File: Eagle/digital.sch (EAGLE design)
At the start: 44 parts, among them J1 USB-B

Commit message: Added indicator LEDs
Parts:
- added LED2, LED3: (no value), led:LED3MM
- added R16, R17: 200k, resistor:R-US_0204/2V
- JP1: device jumper:JP1Q -> jumper:JP2E
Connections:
- new net N$41: LED2.A, R16.1
- new net N$42: LED3.A, R17.1
- new net N$43: J1.VBUS, R17.2
- new net N$45: C3.1, C4.1, C5.1, JP1.2, U$1.VDD$1, U$1.VDD$2
- net +5V/2: now also JP1.3, R16.2; no longer C3.1, C4.1, C5.1, JP1.2, U$1.VDD$1, U$1.VDD$2
- net DGND: now also LED2.C, LED3.C
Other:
- moved on the sheet: C4, C5
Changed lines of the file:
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@@
 <part name="SUPPLY3" library="supply2" deviceset="+5V/2" device=""/>
 <part name="SUPPLY20" library="supply2" deviceset="+5V/2" device=""/>
-<part name="SUPPLY7" library="supply2" deviceset="+5V/2" device=""/>
-<part name="SUPPLY9" library="supply2" deviceset="+5V/2" device=""/>
-<part name="SUPPLY4" library="supply2" deviceset="+5V/2" device=""/>
 <part name="X1" library="con-subd" deviceset="M25?S" device="H"/>
-<part name="JP1" library="jumper" deviceset="JP1Q" device=""/>
 <part name="SUPPLY11" library="supply2" deviceset="+5V/2" device=""/>
 <part name="SUPPLY12" library="supply2" deviceset="GND" device=""/>
@@
 <part name="SUPPLY56" library="supply2" deviceset="DGND" device=""/>
 <part name="SUPPLY57" library="supply2" deviceset="DGND" device=""/>
+<part name="R16" library="resistor" deviceset="R-US_" device="0204/2V" value="200k"/>
+<part name="LED2" library="led" deviceset="LED" device="3MM"/>
+<part name="R17" library="resistor" deviceset="R-US_" device="0204/2V" value="200k"/>
+<part name="LED3" library="led" deviceset="LED" device="3MM"/>
+<part name="SUPPLY58" library="supply2" deviceset="DGND" device=""/>
+<part name="JP1" library="jumper" deviceset="JP2E" device=""/>
 </parts>
 <sheets>
@@
 <instance part="J1" gate="G$1" x="71.12" y="0"/>
 <instance part="C3" gate="G$1" x="45.72" y="111.76"/>
-<instance part="C4" gate="G$1" x="15.24" y="129.54"/>
-<instance part="C5" gate="G$1" x="27.94" y="132.08"/>
+<instance part="C4" gate="G$1" x="-7.62" y="88.9"/>
+<instance part="C5" gate="G$1" x="5.08" y="88.9"/>
 <instance part="SUPPLY13" gate="GND" x="147.32" y="-96.52"/>
 <instance part="CN1" gate="G$1" x="355.6" y="-17.78" rot="MR0"/>
@@
 <instance part="SUPPLY17" gate="G$1" x="35.56" y="-15.24"/>
 <instance part="SUPPLY1" gate="G$1" x="-2.54" y="35.56"/>
-<instance part="SUPPLY5" gate="G$1" x="0" y="91.44"/>
+<instance part="SUPPLY5" gate="G$1" x="-20.32" y="91.44"/>
 <instance part="SUPPLY6" gate="G$1" x="68.58" y="-5.08"/>
-<instance part="SUPPLY8" gate="G$1" x="15.24" y="121.92"/>
-<instance part="SUPPLY10" gate="G$1" x="27.94" y="124.46"/>
+<instance part="SUPPLY8" gate="G$1" x="-7.62" y="78.74"/>
+<instance part="SUPPLY10" gate="G$1" x="5.08" y="78.74"/>
 <instance part="SUPPLY18" gate="G$1" x="325.12" y="-30.48"/>
 <instance part="C12" gate="G$1" x="254" y="-17.78"/>
@@
 <instance part="SUPPLY19" gate="+5V" x="218.44" y="-5.08"/>
 <instance part="SUPPLY3" gate="G$1" x="304.8" y="-5.08"/>
-<instance part="SUPPLY20" gate="G$1" x="35.56" y="111.76"/>
-<instance part="SUPPLY7" gate="G$1" x="15.24" y="134.62"/>
-<instance part="SUPPLY9" gate="G$1" x="27.94" y="137.16"/>
-<instance part="SUPPLY4" gate="G$1" x="-2.54" y="124.46"/>
+<instance part="SUPPLY20" gate="G$1" x="40.64" y="116.84" rot="R270"/>
 <instance part="X1" gate="-1" x="149.86" y="-78.74"/>
 <instance part="X1" gate="-4" x="149.86" y="-81.28"/>
@@
 <instance part="X1" gate="-25" x="-60.96" y="12.7" rot="R180"/>
 <instance part="X1" gate="-17" x="215.9" y="-7.62" rot="R180"/>
-<instance part="JP1" gate="A" x="-2.54" y="114.3"/>
 <instance part="SUPPLY11" gate="G$1" x="106.68" y="124.46"/>
 <instance part="SUPPLY12" gate="GND" x="124.46" y="114.3"/>
@@
 <instance part="SUPPLY56" gate="G$1" x="96.52" y="-2.54"/>
 <instance part="SUPPLY57" gate="G$1" x="96.52" y="-17.78"/>
+<instance part="R16" gate="G$1" x="347.98" y="-12.7" rot="R90"/>
+<instance part="LED2" gate="G$1" x="347.98" y="-20.32"/>
+<instance part="R17" gate="G$1" x="63.5" y="-2.54" rot="R90"/>
+<instance part="LED3" gate="G$1" x="63.5" y="-10.16"/>
+<instance part="SUPPLY58" gate="G$1" x="63.5" y="-17.78"/>
+<instance part="JP1" gate="1" x="35.56" y="119.38"/>
 </instances>
 <busses>
@@
 <segment>
 <pinref part="U$2" gate="G$1" pin="GND"/>
-<wire x1="-33.02" y1="93.98" x2="0" y2="93.98" width="0.1524" layer="91"/>
+<wire x1="-33.02" y1="93.98" x2="-20.32" y2="93.98" width="0.1524" layer="91"/>
 <pinref part="SUPPLY5" gate="G$1" pin="DGND"/>
 </segment>
@@
 <pinref part="C4" gate="G$1" pin="2"/>
 <pinref part="SUPPLY8" gate="G$1" pin="DGND"/>
+<wire x1="-7.62" y1="81.28" x2="-7.62" y2="83.82" width="0.1524" layer="91"/>
 </segment>
 <segment>
 <pinref part="C5" gate="G$1" pin="2"/>
 <pinref part="SUPPLY10" gate="G$1" pin="DGND"/>
+<wire x1="5.08" y1="81.28" x2="5.08" y2="83.82" width="0.1524" layer="91"/>
 </segment>
 <segment>
 <pinref part="CN1" gate="G$1" pin="GND"/>
 <wire x1="353.06" y1="-20.32" x2="353.06" y2="-27.94" width="0.1524" layer="91"/>
-<wire x1="353.06" y1="-27.94" x2="337.82" y2="-27.94" width="0.1524" layer="91"/>
+<wire x1="353.06" y1="-27.94" x2="347.98" y2="-27.94" width="0.1524" layer="91"/>
 <pinref part="D1" gate="G$1" pin="A"/>
+<wire x1="347.98" y1="-27.94" x2="337.82" y2="-27.94" width="0.1524" layer="91"/>
 <wire x1="337.82" y1="-27.94" x2="325.12" y2="-27.94" width="0.1524" layer="91"/>
 <wire x1="337.82" y1="-20.32" x2="337.82" y2="-27.94" width="0.1524" layer="91"/>
@@
 <junction x="312.42" y="-27.94"/>
 <pinref part="SUPPLY18" gate="G$1" pin="DGND"/>
+<pinref part="LED2" gate="G$1" pin="C"/>
+<wire x1="347.98" y1="-25.4" x2="347.98" y2="-27.94" width="0.1524" layer="91"/>
+<junction x="347.98" y="-27.94"/>
 </segment>
 <segment>
@@
 <pinref part="OK7" gate="B" pin="C"/>
 <pinref part="SUPPLY57" gate="G$1" pin="DGND"/>
+</segment>
+<segment>
+<pinref part="LED3" gate="G$1" pin="C"/>
+<pinref part="SUPPLY58" gate="G$1" pin="DGND"/>
 </segment>
 </net>
@@
 <pinref part="CN1" gate="G$1" pin="PWR"/>
 <wire x1="353.06" y1="-15.24" x2="353.06" y2="-7.62" width="0.1524" layer="91"/>
-<wire x1="353.06" y1="-7.62" x2="337.82" y2="-7.62" width="0.1524" layer="91"/>
+<wire x1="353.06" y1="-7.62" x2="347.98" y2="-7.62" width="0.1524" layer="91"/>
 <pinref part="D1" gate="G$1" pin="C"/>
+<wire x1="347.98" y1="-7.62" x2="337.82" y2="-7.62" width="0.1524" layer="91"/>
 <wire x1="337.82" y1="-7.62" x2="325.12" y2="-7.62" width="0.1524" layer="91"/>
 <wire x1="337.82" y1="-15.24" x2="337.82" y2="-7.62" width="0.1524" layer="91"/>
@@
 <pinref part="SUPPLY3" gate="G$1" pin="+5V/2"/>
 <junction x="304.8" y="-7.62"/>
-</segment>
-<segment>
-<pinref part="U$1" gate="G$1" pin="VDD$1"/>
-<wire x1="35.56" y1="109.22" x2="35.56" y2="106.68" width="0.1524" layer="91"/>
-<pinref part="U$1" gate="G$1" pin="VDD$2"/>
-<wire x1="35.56" y1="106.68" x2="38.1" y2="106.68" width="0.1524" layer="91"/>
-<junction x="35.56" y="106.68"/>
-<wire x1="38.1" y1="106.68" x2="40.64" y2="106.68" width="0.1524" layer="91"/>
-<wire x1="40.64" y1="106.68" x2="40.64" y2="114.3" width="0.1524" layer="91"/>
-<junction x="38.1" y="106.68"/>
-<pinref part="C3" gate="G$1" pin="1"/>
-<wire x1="40.64" y1="114.3" x2="45.72" y2="114.3" width="0.1524" layer="91"/>
-<pinref part="SUPPLY20" gate="G$1" pin="+5V/2"/>
-</segment>
-<segment>
-<pinref part="C4" gate="G$1" pin="1"/>
-<pinref part="SUPPLY7" gate="G$1" pin="+5V/2"/>
-</segment>
-<segment>
-<pinref part="C5" gate="G$1" pin="1"/>
-<pinref part="SUPPLY9" gate="G$1" pin="+5V/2"/>
-</segment>
-<segment>
-<pinref part="JP1" gate="A" pin="2"/>
-<pinref part="SUPPLY4" gate="G$1" pin="+5V/2"/>
+<pinref part="R16" gate="G$1" pin="2"/>
+<junction x="347.98" y="-7.62"/>
 </segment>
 <segment>
@@
 <pinref part="SUPPLY47" gate="G$1" pin="+5V/2"/>
 </segment>
+<segment>
+<pinref part="SUPPLY20" gate="G$1" pin="+5V/2"/>
+<pinref part="JP1" gate="1" pin="3"/>
+</segment>
 </net>
 <net name="N$10" class="0">
 <segment>
 <pinref part="U$2" gate="G$1" pin="VCC"/>
-<pinref part="JP1" gate="A" pin="1"/>
 <wire x1="-33.02" y1="96.52" x2="-2.54" y2="96.52" width="0.1524" layer="91"/>
-<wire x1="-2.54" y1="96.52" x2="-2.54" y2="106.68" width="0.1524" layer="91"/>
+<wire x1="-2.54" y1="96.52" x2="-2.54" y2="109.22" width="0.1524" layer="91"/>
+<wire x1="33.02" y1="116.84" x2="33.02" y2="109.22" width="0.1524" layer="91"/>
+<wire x1="33.02" y1="109.22" x2="-2.54" y2="109.22" width="0.1524" layer="91"/>
+<pinref part="JP1" gate="1" pin="1"/>
 </segment>
 </net>
@@
 </segment>
 </net>
+<net name="N$41" class="0">
+<segment>
+<pinref part="R16" gate="G$1" pin="1"/>
+<pinref part="LED2" gate="G$1" pin="A"/>
+</segment>
+</net>
+<net name="N$42" class="0">
+<segment>
+<pinref part="R17" gate="G$1" pin="1"/>
+<pinref part="LED3" gate="G$1" pin="A"/>
+</segment>
+</net>
+<net name="N$43" class="0">
+<segment>
+<pinref part="J1" gate="G$1" pin="VBUS"/>
+<pinref part="R17" gate="G$1" pin="2"/>
+<wire x1="68.58" y1="2.54" x2="63.5" y2="2.54" width="0.1524" layer="91"/>
+</segment>
+</net>
+<net name="N$45" class="0">
+<segment>
+<pinref part="C4" gate="G$1" pin="1"/>
+<pinref part="C5" gate="G$1" pin="1"/>
+<wire x1="-7.62" y1="91.44" x2="2.54" y2="91.44" width="0.1524" layer="91"/>
+<wire x1="2.54" y1="91.44" x2="5.08" y2="91.44" width="0.1524" layer="91"/>
+<wire x1="2.54" y1="91.44" x2="2.54" y2="106.68" width="0.1524" layer="91"/>
+<junction x="2.54" y="91.44"/>
+<pinref part="U$1" gate="G$1" pin="VDD$1"/>
+<pinref part="U$1" gate="G$1" pin="VDD$2"/>
+<wire x1="35.56" y1="106.68" x2="38.1" y2="106.68" width="0.1524" layer="91"/>
+<wire x1="38.1" y1="106.68" x2="40.64" y2="106.68" width="0.1524" layer="91"/>
+<wire x1="40.64" y1="106.68" x2="40.64" y2="114.3" width="0.1524" layer="91"/>
+<junction x="38.1" y="106.68"/>
+<pinref part="C3" gate="G$1" pin="1"/>
+<wire x1="40.64" y1="114.3" x2="45.72" y2="114.3" width="0.1524" layer="91"/>
+<pinref part="JP1" gate="1" pin="2"/>
+<wire x1="35.56" y1="116.84" x2="35.56" y2="106.68" width="0.1524" layer="91"/>
+<junction x="35.56" y="106.68"/>
+<wire x1="2.54" y1="106.68" x2="35.56" y2="106.68" width="0.1524" layer="91"/>
+</segment>
+</net>

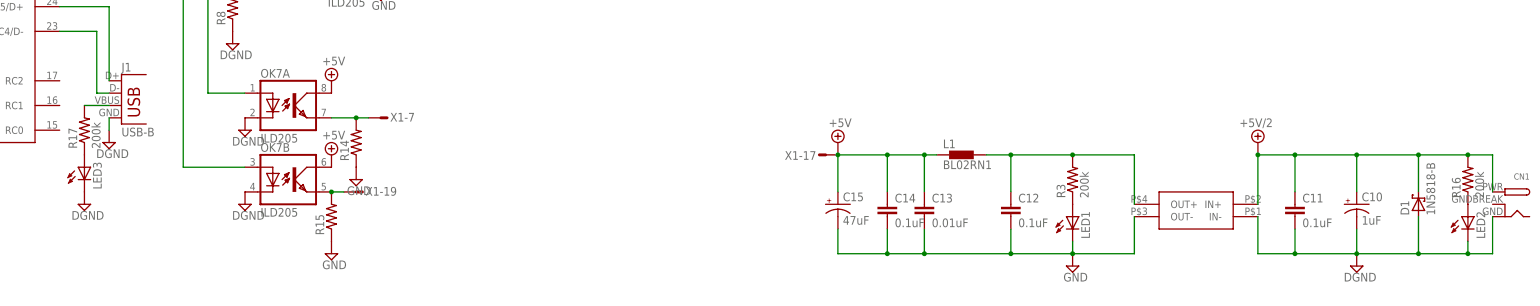
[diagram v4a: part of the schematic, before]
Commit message: Updated resistor values
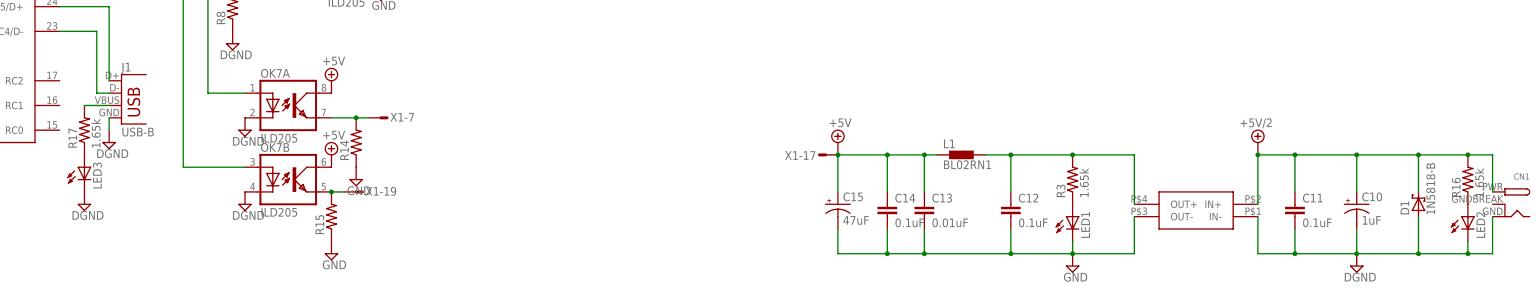
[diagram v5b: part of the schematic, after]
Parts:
- R16, R17, R3: value 200k -> 1.65k
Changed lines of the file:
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@@
 <part name="C11" library="resistor" deviceset="C-EU" device="050-025X075" value="0.1uF"/>
 <part name="U$3" library="modEEG" deviceset="ROL-0505S" device=""/>
-<part name="R3" library="resistor" deviceset="R-US_" device="0204/2V" value="200k"/>
+<part name="R3" library="resistor" deviceset="R-US_" device="0204/2V" value="1.65k"/>
 <part name="LED1" library="led" deviceset="LED" device="3MM"/>
 <part name="SUPPLY2" library="supply2" deviceset="GND" device=""/>
@@
 <part name="SUPPLY56" library="supply2" deviceset="DGND" device=""/>
 <part name="SUPPLY57" library="supply2" deviceset="DGND" device=""/>
-<part name="R16" library="resistor" deviceset="R-US_" device="0204/2V" value="200k"/>
+<part name="R16" library="resistor" deviceset="R-US_" device="0204/2V" value="1.65k"/>
 <part name="LED2" library="led" deviceset="LED" device="3MM"/>
-<part name="R17" library="resistor" deviceset="R-US_" device="0204/2V" value="200k"/>
+<part name="R17" library="resistor" deviceset="R-US_" device="0204/2V" value="1.65k"/>
 <part name="LED3" library="led" deviceset="LED" device="3MM"/>
 <part name="SUPPLY58" library="supply2" deviceset="DGND" device=""/>

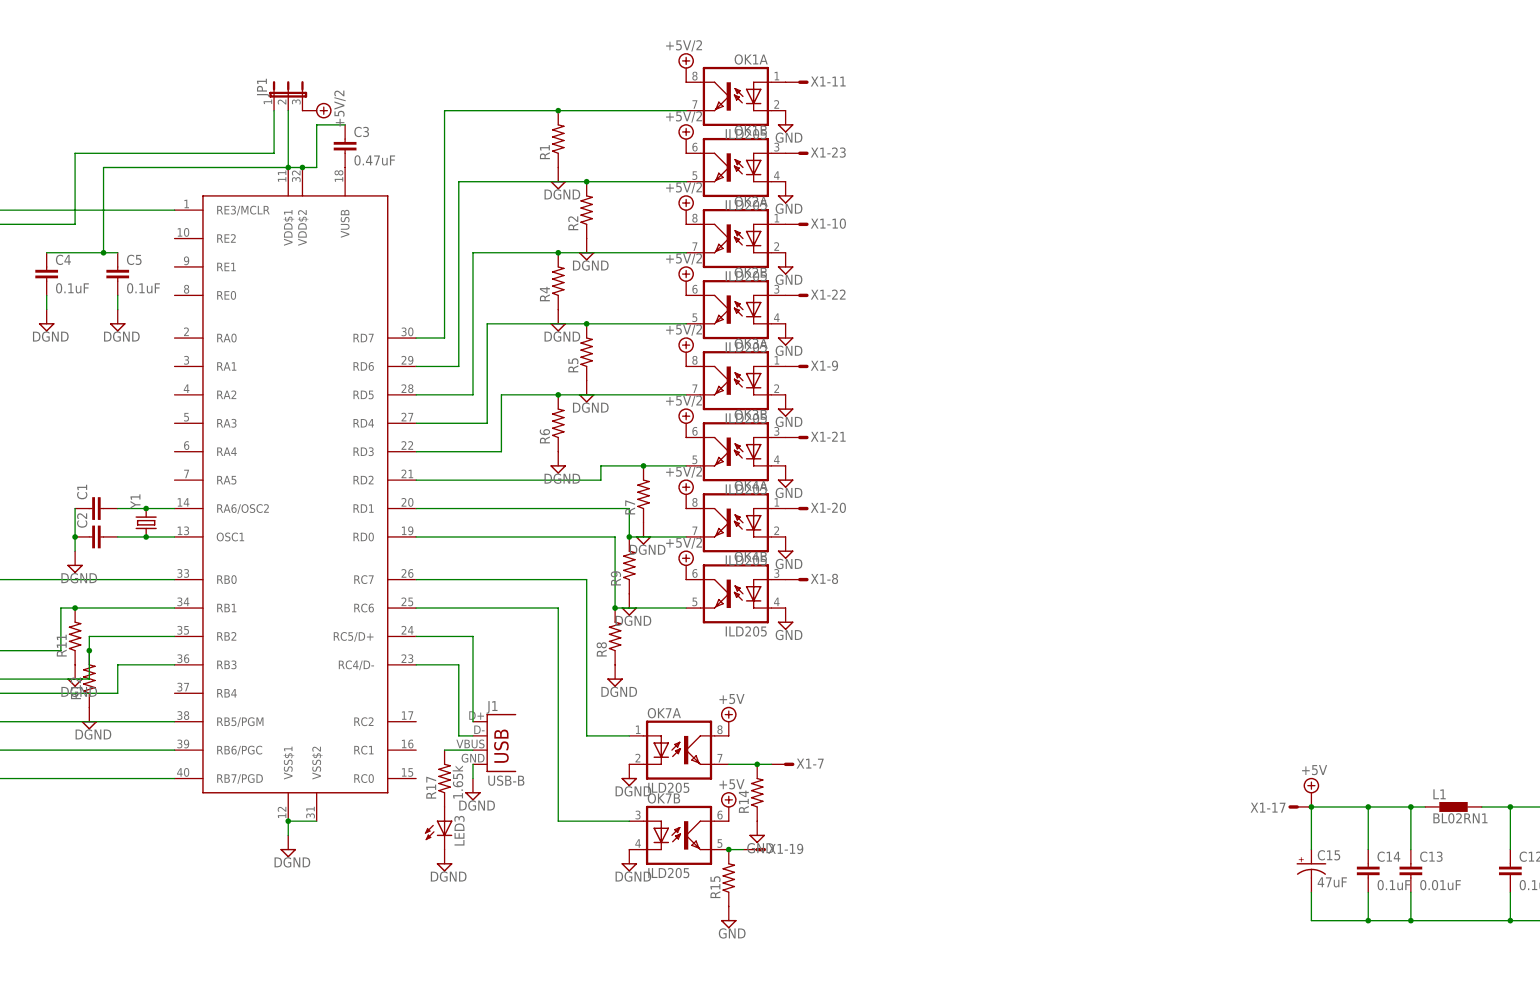
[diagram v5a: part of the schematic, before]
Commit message: Added 232 interface
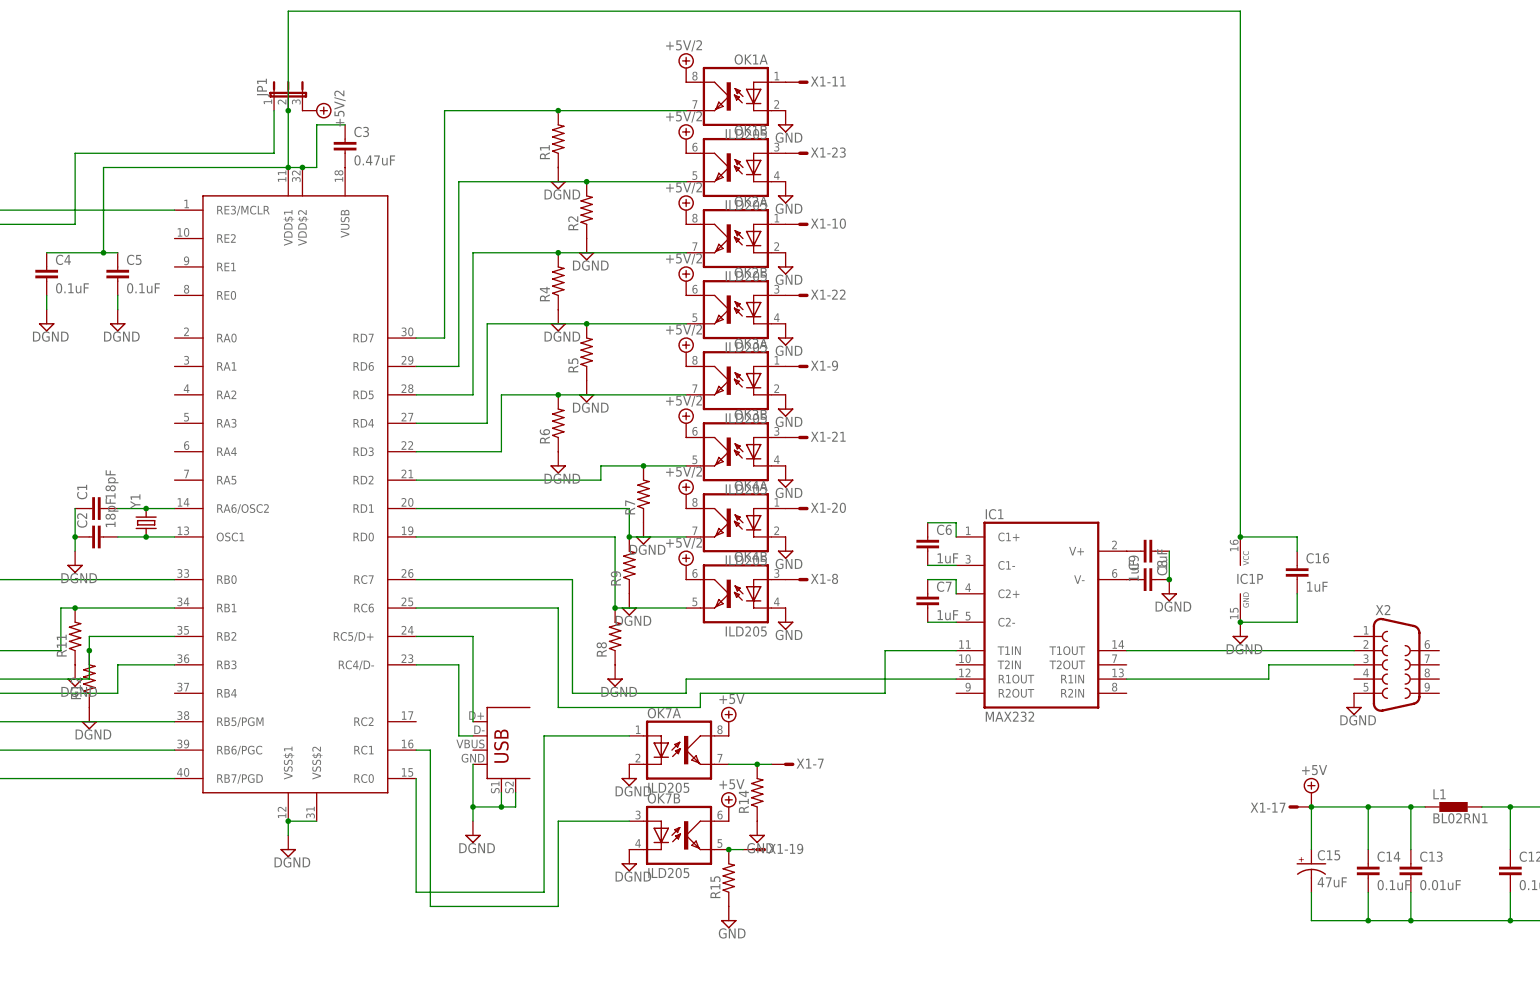
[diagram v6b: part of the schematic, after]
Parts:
- removed LED3: (no value), led:LED3MM
- removed R17: 1.65k, resistor:R-US_0204/2V
- added C16, C6, C7, C8, C9: 1uF, resistor:C-EU050-025X075
- added IC1: MAX232, maxim:MAX232
- added X2: (no value), con-subd:F09HP
- C1, C2: value (none) -> 18pF
- J1: value USB-B -> USB+SHIELD; device SparkFun-Connectors:USBPTH -> SparkFun-Connectors:USB+SHIELD
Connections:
- removed net N$42: LED3.A, R17.1
- removed net N$43: J1.VBUS, R17.2
- new net N$44: IC1G$1.T1IN, U$1.RC6
- new net N$46: IC1G$1.R1OUT, U$1.RC7
- new net N$47: C8.2, IC1G$1.V+
- new net N$48: C9.1, IC1G$1.V-
- new net N$49: C6.2, IC1G$1.C1-
- new net N$50: C6.1, IC1G$1.C1+
- new net N$51: C7.1, IC1G$1.C2+
- new net N$52: C7.2, IC1G$1.C2-
- new net N$53: IC1G$1.R1IN, X2.3
- new net N$54: IC1G$1.T1OUT, X2.2
- net DGND: now also C16.2, C8.1, C9.2, IC1P.GND, J1.S1, J1.S2, X2.5; no longer LED3.C
- net N$39: now also U$1.RC0; no longer U$1.RC7
- net N$40: now also U$1.RC1; no longer U$1.RC6
- net N$45: now also C16.1, IC1P.VCC

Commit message: Changed USB to differential pair
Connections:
- net N$3 renamed USB_P
- net N$4 renamed USB_N
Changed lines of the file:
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@@
 <class number="0" name="default" width="0" drill="0">
+</class>
+<class number="1" name="USB" width="0.3048" drill="0">
+<clearance class="1" value="2.54"/>
 </class>
 </classes>
@@
 </segment>
 </net>
-<net name="N$3" class="0">
+<net name="USB_P" class="1">
 <segment>
 <pinref part="J1" gate="G$1" pin="D+"/>
@@
 </segment>
 </net>
-<net name="N$4" class="0">
+<net name="USB_N" class="1">
 <segment>
 <pinref part="U$1" gate="G$1" pin="RC4/D-"/>

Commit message: Added ethernet module
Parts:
- removed C16, C6, C7, C8, C9: 1uF, resistor:C-EU050-025X075
- removed J1: USB+SHIELD, SparkFun-Connectors:USB+SHIELD
- removed X2: (no value), con-subd:F09HP
- added S1: (no value), switch:9070-1W
- added U$4: ENC28J60-H, modEEG:ENC28J60-H
- added U$5: USBSMD, SparkFun-Connectors:USBSMD
- IC1: value MAX232 -> L4931CZ33-AP; device maxim:MAX232 -> v-reg:LP2950ACZ-3.0
- U$2: value PIC-ICSPPOLAR_LOCK -> PIC-ICSPPTH; device SparkFun-Connectors:PIC-ICSPPOLAR_LOCK -> SparkFun-Connectors:PIC-ICSPPTH
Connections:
- removed net N$46: IC1G$1.R1OUT, U$1.RC7
- removed net N$47: C8.2, IC1G$1.V+
- removed net N$48: C9.1, IC1G$1.V-
- removed net N$49: C6.2, IC1G$1.C1-
- removed net N$50: C6.1, IC1G$1.C1+
- removed net N$51: C7.1, IC1G$1.C2+
- removed net N$52: C7.2, IC1G$1.C2-
- removed net N$53: IC1G$1.R1IN, X2.3
- removed net N$54: IC1G$1.T1OUT, X2.2
- new net N$3: U$1.RC7, U$4.MOSI
- new net N$4: IC1.OUT, U$4.3V3
- new net N$42: U$1.RB1, U$4.SCK
- new net N$43: U$1.RA5, U$4.CS
- net +5V/2: now also IC1.IN, S1.P; no longer CN1.PWR
- net DGND: now also IC1.GND, S1.B, S1.B1, S1.S, U$4.GND; no longer C16.2, C8.1, C9.2, IC1P.GND, J1.GND, J1.S1, J1.S2, X2.5
- net N$33: now also U$1.RB2; no longer U$1.RB0
- net N$34: now also U$1.RB3; no longer U$1.RB1
- net N$35: now also U$1.RB4; no longer U$1.RB2
- net N$36: now also U$1.RB5/PGM; no longer U$1.RB3
- net N$44: now also CN1.PWR, S1.O; no longer IC1G$1.T1IN, U$1.RC6
- net N$45: no longer C16.1, IC1P.VCC
- net N$6: now also U$1.RB0, U$4.MISO; no longer U$1.RB5/PGM, U$2.PGM
- net USB_N: now also U$5.D-; no longer J1.D-
- net USB_P: now also U$5.D+; no longer J1.D+
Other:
- moved on the sheet: CN1, OK1A, OK1B, OK2A, OK2B, OK3A, OK3B, OK4A, OK4B, R1, R11, R12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
